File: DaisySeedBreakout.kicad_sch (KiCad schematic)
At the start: 48 parts, among them J2 Conn_01x02, J24 Conn_01x02, J25 Conn_01x02, J26 Conn_02x04, J30 Conn_01x02, J31 Conn_02x04, J32 Conn_01x02, J33 Conn_01x02, J34 Conn_01x02, J35 Conn_01x02, J6 Conn_01x02, J7 Conn_01x02, U10 TPD2EUSB30ADRTR, U11 TPS560200DBVR

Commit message: getting closer
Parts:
- removed C61: 47uF, Capacitor_SMD:C_0805_2012Metric, symbol Device:C
- removed C62, C65: 0.1uF, Capacitor_SMD:C_0402_1005Metric, symbol Device:C
- removed C63, C64: 10uF, Capacitor_SMD:C_0603_1608Metric, symbol Device:C
- removed J26: Conn_02x04, Connector_PinHeader_2.54mm:PinHeader_2x04_P2.54mm_Vertical, symbol 4ms_Connector:Conn_02x04
- removed J32, J33, J34, J7: Conn_01x02, Connector_PinHeader_2.54mm:PinHeader_1x02_P2.54mm_Vertical, symbol 4ms_Connector:Conn_01x02
- removed L1: 10uH 1.9A ASPI-0628-100M-T1, 10uHInductor:ASPI-0628_ASPI-0628-4R7M-T1_ABR, symbol Device:L_Small
- removed R59, R60, R63, R64: TBD, Resistor_SMD:R_0402_1005Metric, symbol Device:R_US
- removed R61: 2.2k, Resistor_SMD:R_0402_1005Metric, symbol Device:R_US
- removed U11: TPS560200DBVR, DBV0005A_N, symbol 2023-10-05_01-44-07:TPS560200DBVR
- added J15: Conn_01x03, Ultralibrarian:PinHeader_1x03_P2.54mm_Vertical_Female, symbol 4ms_Connector:Conn_01x03
- added J16: Conn_02x04, Connector_PinHeader_2.54mm:PinHeader_2x04_P2.54mm_Vertical, symbol 4ms_Connector:Conn_02x04
- renumbered R56 to Z56
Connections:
- net GND: now also H1.1, H2.1, H3.1, H4.1, J15.1 (Pin_1), J16.1 (Pin_1), J16.3 (Pin_3), J16.5 (Pin_5), J16.7 (Pin_7)
- net USB_n: now also J15.3 (Pin_3)
- net USB_p: now also J15.2 (Pin_2)
- net at C57.1, C58.1, CR1.1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: now also J16.2 (Pin_2), J16.4 (Pin_4), J16.6 (Pin_6), J16.8 (Pin_8)
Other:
- sheet Audio Out ports: added none; removed ENABLE_10V_EURO_N, VCC_4V5_36V
- note added: "Make line to Eurorack and Eurorack to line converter. Then make everything line on the product. make CV and gate easy to hook up though? Or provide PCB to convert AI/AO to CV voltages too? Make 12V to 5V module?"
- note removed: "1.16V Threshold 7V Max allowed"
- note removed: "5V"
- note removed: "Current limiting provided by power supply. This is only thing on 5V."
- note removed: "Header to enable Eurorack mode"
- moved on the sheet: C57, C58, C59, C60, CR1, J31, J35, J5, Z56

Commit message: trying grid of female headers to reduce header count and enable plug in modules
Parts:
- removed J16, J31: Conn_02x04, Connector_PinHeader_2.54mm:PinHeader_2x04_P2.54mm_Vertical, symbol 4ms_Connector:Conn_02x04
- removed J24, J25, J30: Conn_01x02, Connector_PinHeader_2.54mm:PinHeader_1x02_P2.54mm_Vertical, symbol 4ms_Connector:Conn_01x02
- added J10, J11, J8, J9: Conn_01x02, 1x2FemaleVertical:PinHeader_1x02_P2.54mm_VerticalFemale, symbol 4ms_Connector:Conn_01x02
- added J17, J19, J23, J26, J27, J28, J29, J7: Pins_02x10_P2.54mm_TH, 2x10FemaleHeader:PinHeader_2x10_P2.54mm_Vertical, symbol Ultralibrarian_modified_symbols:Pins_02x10_P2.54mm_TH
- J2, J35, J6: footprint Connector_PinHeader_2.54mm:PinHeader_1x02_P2.54mm_Vertical -> 1x2FemaleVertical:PinHeader_1x02_P2.54mm_VerticalFemale
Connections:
- net +12V: now also J10.1 (Pin_1), J10.2 (Pin_2), J11.1 (Pin_1), J11.2 (Pin_2)
- net +3.3V: now also J9.1 (Pin_1)
- net Audio Out/AUDIO_OUT_L_EXT: no longer J6.1 (Pin_1)
- net GND: now also J9.2 (Pin_2)
- net at J35.1 (Pin_1), J5.1 (IN1), J5.2 (IN2): now also J6.1 (Pin_1)
- net AI0 renamed CONN_1_AI_DIO0
- net AI1 renamed CONN_2_AI_DIO0
- net AI10 renamed CONN_9_AI_DIO0
- net AI11 renamed CONN_10_AI_DIO0
- net AI2 renamed CONN_3_AI_DIO0
- net AI3 renamed CONN_4_AI_DIO0
- net AI4 renamed CONN_5_AI_DIO0
- net AI5 renamed CONN_6_AI_DIO0
- net AI6 renamed CONN_7_AI_DIO0
- net AI9 renamed CONN_8_AI_DIO0
- net AO0: no longer names the net of A1.29 (DAC_OUT2)
- net AO1: no longer names the net of A1.30 (DAC_OUT1)
- net GPIO_Conn/GPIO_Conn renamed arduino_coprocessor/I2C0_SCL
- net GPIO_Conn1/GPIO_Conn renamed arduino_coprocessor/I2C0_SDA
- net GPIO_Conn11/GPIO_Conn: no longer names the net of A1.12 (I2C1_SCL), R11.2
- net GPIO_Conn11/GPIO_Conn: now also J8.1 (Pin_1)
- net GPIO_Conn12/GPIO_Conn: no longer names the net of A1.13 (I2C1_SDA), R6.2
- net GPIO_Conn12/GPIO_Conn: now also J8.2 (Pin_2)
- net GPIO_Conn2/GPIO_Conn renamed arduino_coprocessor/I2C2_SCL
- net GPIO_Conn3/GPIO_Conn renamed arduino_coprocessor/I2C2_SDA
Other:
- removed sheet AI_GPIO
- removed sheet AI_GPIO1
- removed sheet AI_GPIO10
- removed sheet AI_GPIO11
- removed sheet AI_GPIO12
- removed sheet AI_GPIO13
- removed sheet AI_GPIO14
- removed sheet AI_GPIO15
- removed sheet AI_GPIO16
- removed sheet AI_GPIO17
- removed sheet AI_GPIO18
- removed sheet AI_GPIO19
- removed sheet AI_GPIO2
- removed sheet AI_GPIO3
- removed sheet AI_GPIO4
- removed sheet AI_GPIO5
- removed sheet AI_GPIO6
- removed sheet AI_GPIO7
- removed sheet AI_GPIO8
- removed sheet AI_GPIO9
- removed sheet Analog_out_conn
- removed sheet Analog_out_conn1
- removed sheet GPIO_Conn
- removed sheet GPIO_Conn1
- removed sheet GPIO_Conn11
- removed sheet GPIO_Conn12
- removed sheet GPIO_Conn2
- removed sheet GPIO_Conn3
- removed sheet GPIO_Conn4
- removed sheet GPIO_Conn5
- removed sheet GPIO_Conn6
- removed sheet GPIO_Conn7
- removed sheet GPIO_Conn8
- removed sheet GPIO_Conn9
- note removed: "3.3V"
- note removed: "VOUT_Protected"
- moved on the sheet: J2

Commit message: simplified design, rely on external boards more to cover those cases
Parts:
- removed C57, C58, C59: 0.1uF, Capacitor_SMD:C_0402_1005Metric, symbol Device:C
- removed C60: 47uF, Capacitor_SMD:C_0805_2012Metric, symbol Device:C
- removed CR1: DFLT15A-7, ZDO_POWERDI123_DIO, symbol 2023-10-02_00-55-35:DFLT15A-7
- removed J10, J35, J6: Conn_01x02, 1x2FemaleVertical:PinHeader_1x02_P2.54mm_VerticalFemale, symbol 4ms_Connector:Conn_01x02
- removed J17, J19, J23, J26, J27, J28, J29, J7: Pins_02x10_P2.54mm_TH, 2x10FemaleHeader:PinHeader_2x10_P2.54mm_Vertical, symbol Ultralibrarian_modified_symbols:Pins_02x10_P2.54mm_TH
- removed J18: ~, Ultralibrarian:STX-4235-3-3-N, symbol Ultralibrarian_modified_symbols:STX-4235-3-3-N
- removed J5: ~, Ultralibrarian:BladeFuseHolder, symbol Ultralibrarian_modified_symbols:BladeFuseHolder
- removed R48, R49, R50, R51: 10k, Resistor_SMD:R_0402_1005Metric, symbol Device:R_US
- removed Z56: RSX501LAM20TR, DIO_RB050LAM_ROM, symbol 2023-10-01_23-34-18:RSX501LAM20TR
- added C10, C2, C8: 0.1uF, Capacitor_SMD:C_0402_1005Metric, symbol Device:C
- added J10, J14: Conn_01x03, Ultralibrarian:PinHeader_1x03_P2.54mm_Vertical_Female, symbol 4ms_Connector:Conn_01x03
- added J12, J13: Conn_01x02, 1x2FemaleVertical:PinHeader_1x02_P2.54mm_VerticalFemale, symbol 4ms_Connector:Conn_01x02
- added J5: Conn_02x08, Connector_PinHeader_2.54mm:PinHeader_2x08_P2.54mm_Vertical, symbol 4ms_Connector:Conn_02x08
- added J6: Pins_02x10_P2.54mm_TH, Connector_PinHeader_2.54mm:PinHeader_2x10_P2.54mm_Vertical, symbol Ultralibrarian_modified_symbols:Pins_02x10_P2.54mm_TH
- added J7: Conn_01x10, Connector_PinHeader_2.54mm:PinHeader_1x10_P2.54mm_Vertical, symbol Connector_Generic:Conn_01x10
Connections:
- net ClassD_20W_Amp/OUT_N is gone; now on net GND: J2.2 (Pin_2)
- net ClassD_20W_Amp/OUT_P is gone; now on net Audio Out/AUDIO_OUT_L_EXT: J2.1 (Pin_1)
- net +12V: no longer J11.1 (Pin_1), J11.2 (Pin_2)
- net +3.3V: no longer J9.1 (Pin_1)
- net +3.3VA: now also C10.1, C2.1, C8.1, J10.3 (Pin_3), J14.3 (Pin_3), J7.1 (Pin_1), J7.10 (Pin_10), J7.2 (Pin_2), J7.3 (Pin_3), J7.4 (Pin_4), J7.5 (Pin_5), J7.6 (Pin_6), J7.7 (Pin_7), J7.8 (Pin_8), J7.9 (Pin_9)
- net Audio In Sum/AUDIO_IN_L_CONN: now also J12.1 (Pin_1)
- net Audio In Sum/AUDIO_IN_R_CONN: now also J13.1 (Pin_1)
- net Audio Out/AUDIO_OUT_R_EXT: now also J11.1 (Pin_1)
- net GND: now also J11.2 (Pin_2), J8.2 (Pin_2), C10.2, C2.2, C8.2, J10.1 (Pin_1), J12.2 (Pin_2), J13.2 (Pin_2), J14.1 (Pin_1), J5.1 (P1), J5.11 (GND), J5.13 (-12), J5.15 (-12V), J5.3 (P3), J5.5 (+12V), J5.7 (12V), J5.9 (GND), J6.1, J6.11, J6.13, J6.15, J6.17, J6.19, J6.3, J6.5, J6.7, J6.9
- net DIO2: now reaches A1.12 (I2C1_SCL), R11.2
- net DIO2: now also J5.6 (P6); no longer J8.1 (Pin_1)
- net DIO3: now reaches A1.13 (I2C1_SDA), R6.2
- net DIO3: now also J5.8 (+12V); no longer J8.2 (Pin_2)
- net AO_0: now reaches A1.29 (DAC_OUT2)
- net AO_0: now also J10.2 (Pin_2)
- net AO_1: now reaches A1.30 (DAC_OUT1)
- net AO_1: now also J14.2 (Pin_2)
- net CONN_10_AI_DIO0 renamed AI_9
- net AI_9: now also J6.20
- net CONN_1_AI_DIO0 renamed AI_0
- net AI_0: now also J6.2
- net CONN_2_AI_DIO0 renamed AI_1
- net AI_1: now also J6.4
- net CONN_3_AI_DIO0 renamed AI_2
- net AI_2: now also J6.6
- net CONN_4_AI_DIO0 renamed AI_3
- net AI_3: now also J6.8
- net CONN_5_AI_DIO0 renamed AI_4
- net AI_4: now also J6.10
- net CONN_6_AI_DIO0 renamed AI_5
- net AI_5: now also J6.12
- net CONN_7_AI_DIO0 renamed AI_6
- net AI_6: now also J6.14
- net CONN_8_AI_DIO0 renamed AI_7
- net AI_7: now also J6.16
- net CONN_9_AI_DIO0 renamed AI_8
- net AI_8: now also J6.18
- net RESET_n renamed DIO0
- net DIO0: now also J5.2 (P2)
- net UPDI renamed DIO1
- net DIO1: now also J5.4 (P4)
- net arduino_coprocessor/SPI0_CS renamed DIO4
- net DIO4: now also J5.10 (GND)
- net arduino_coprocessor/SPI0_SCLK renamed DIO5
- net DIO5: now also J5.12 (GND)
- net arduino_coprocessor/UART0_RXD_SPI0_MISO renamed DIO6
- net DIO6: now also J5.14 (-12V)
- net arduino_coprocessor/UART0_TXD_SPI0_MOSI renamed DIO7
- net DIO7: now also J5.16 (P16)
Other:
- removed sheet ClassD_20W_Amp
- removed sheet arduino_coprocessor
- note added: "These two connectors go side by side to make a 3 wide connector"
- note removed: "Audio In"
- note removed: "Audio Out"
- note removed: "Header for a speaker"
- note removed: "VIN"
- moved on the sheet: J15, J2, U10

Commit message: started layout
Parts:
- added J16: Conn_01x02, 1x2FemaleVertical:PinHeader_1x02_P2.54mm_VerticalFemale, symbol 4ms_Connector:Conn_01x02
- A1: footprint Module:Electrosmith_Daisy_Seed -> ElectgrosmithSurfaceMountModule:Electrosmith_Daisy_Seed
- C6: footprint Capacitor_SMD:C_0603_1608Metric -> Capacitor_SMD:C_0402_1005Metric; Specs 0603, 16V -> (none)
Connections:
- net +3.3V: now also J16.1 (Pin_1)
- net +3.3VA: now also C6.1, J8.1 (Pin_1)
- net DIO0: now also A1.12 (I2C1_SCL), R11.2; no longer A1.33 (SAI2_SD_A)
- net DIO1: now also A1.13 (I2C1_SDA), R6.2; no longer A1.34 (SAI2_FS)
- net DIO2: now also A1.8 (SPI1_CS); no longer A1.12 (I2C1_SCL), R11.2
- net DIO3: now also A1.9 (SPI1_SCK); no longer A1.13 (I2C1_SDA), R6.2
- net DIO4: now also A1.10 (SPI1_POCI); no longer A1.8 (SPI1_CS)
- net DIO5: now also A1.11 (SPI1_PICO); no longer A1.9 (SPI1_SCK)
- net DIO6: now also A1.33 (SAI2_SD_A); no longer A1.10 (SPI1_POCI)
- net DIO7: now also A1.34 (SAI2_FS); no longer A1.11 (SPI1_PICO)
- net GND: now also J16.2 (Pin_2)
- net Audio In Sum/AUDIO_IN_R_LOCAL: now reaches J9.1 (Pin_1)
- net +12V: no longer names the net of A1.39 (VIN)
- net +12V: no longer C6.1
- no-connect marks 0 -> 1
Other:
- moved on the sheet: J9

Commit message: periodic update
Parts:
- removed J6: Pins_02x10_P2.54mm_TH, Connector_PinHeader_2.54mm:PinHeader_2x10_P2.54mm_Vertical, symbol Ultralibrarian_modified_symbols:Pins_02x10_P2.54mm_TH
- removed J7: Conn_01x10, Connector_PinHeader_2.54mm:PinHeader_1x10_P2.54mm_Vertical, symbol Connector_Generic:Conn_01x10
- removed J9: Conn_01x02, 1x2FemaleVertical:PinHeader_1x02_P2.54mm_VerticalFemale, symbol 4ms_Connector:Conn_01x02
- added J9: Pins_02x10_P2.54mm_TH, HeadersWithSolderHoles:PinHeader_3x10_P2.54mm_Vertical, symbol 3x10HeaderWithSolderHoles:Pins_03x10_P2.54mm_TH_SolderHoles
- J10, J14, J15: footprint Ultralibrarian:PinHeader_1x03_P2.54mm_Vertical_Female -> HeadersWithSolderHoles:PinHeader_1x03_P2.54mm_Vertical_Female_WithSolderHoles
- J11, J12, J13, J2: footprint 1x2FemaleVertical:PinHeader_1x02_P2.54mm_VerticalFemale -> HeadersWithSolderHoles:PinHeader_1x02_P2.54mm_VerticalFemale_WithSolderHoles
- J5: footprint Connector_PinHeader_2.54mm:PinHeader_2x08_P2.54mm_Vertical -> HeadersWithSolderHoles:PinHeader_2x08_P2.54mm_Vertical_Female
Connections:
- net +3.3V: now also J16.2 (Pin_2); no longer J16.1 (Pin_1)
- net +3.3VA: now also J9.1, J9.10, J9.2, J9.3, J9.4, J9.5, J9.6, J9.7, J9.8, J9.9; no longer J8.1 (Pin_1)
- net AI_0: now also J9.11
- net AI_1: now also J9.12
- net AI_2: now also J9.13
- net AI_3: now also J9.14
- net AI_4: now also J9.15
- net AI_5: now also J9.16
- net AI_6: now also J9.17
- net AI_7: now also J9.18
- net AI_8: now also J9.19
- net AI_9: now also J9.20
- net Audio In/AUDIO_IN_L_CONN: now also J8.2 (Pin_2)
- net DIO0: now also J5.16 (P16); no longer J5.2 (P2)
- net DIO1: now also J5.14 (-12V); no longer J5.4 (P4)
- net DIO2: now also J5.12 (GND); no longer J5.6 (P6)
- net DIO3: now also J5.10 (GND); no longer J5.8 (+12V)
- net DIO4: now also J5.8 (+12V); no longer J5.10 (GND)
- net DIO5: now also J5.6 (P6); no longer J5.12 (GND)
- net DIO6: now also J5.4 (P4); no longer J5.14 (-12V)
- net DIO7: now also J5.2 (P2); no longer J5.16 (P16)
- net GND: now also J16.1 (Pin_1), J9.21, J9.22, J9.23, J9.24, J9.25, J9.26, J9.27, J9.28, J9.29, J9.30; no longer J16.2 (Pin_2), J8.2 (Pin_2)
- net USB_n: now also J15.2 (Pin_2); no longer J15.3 (Pin_3)
- net USB_p: now also J15.3 (Pin_3); no longer J15.2 (Pin_2)
- new net Condensor Microphone/AUDIO_OUT: J8.1 (Pin_1)
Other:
- sheet Audio In Sum renamed Audio In
- sheet Audio In ports: added none; removed AUDIO_IN_L_LOCAL, AUDIO_IN_R_LOCAL
- sheet Audio Out ports: added VCC; removed none
- note added: "Nice Looking LEDs Adjust audio input gain"
- note added: "Short header to feed mic through"
- note removed: "Accelerometer/Magnometer/Gyroscope/Temperature Sensor"
- note removed: "Eurorack +-10V compatibility? Add op amp that can be configured for either?"
- note removed: "Make line to Eurorack and Eurorack to line converter. Then make everything line on the product. make CV and gate easy to hook up though? Or provide PCB to convert AI/AO to CV voltages too? Make 12V to 5V module?"
- note removed: "Microphone"
- note removed: "NIce Looking LEDs"
- note removed: "Power/Battery connector/Input protection"
- note removed: "Speaker Driver"
- note removed: "Sprinkle Decoupling Bulk Decoupling"
- note removed: "These two connectors go side by side to make a 3 wide connector"
- note removed: "USB Host"
- moved on the sheet: C2, C6, C8, J5

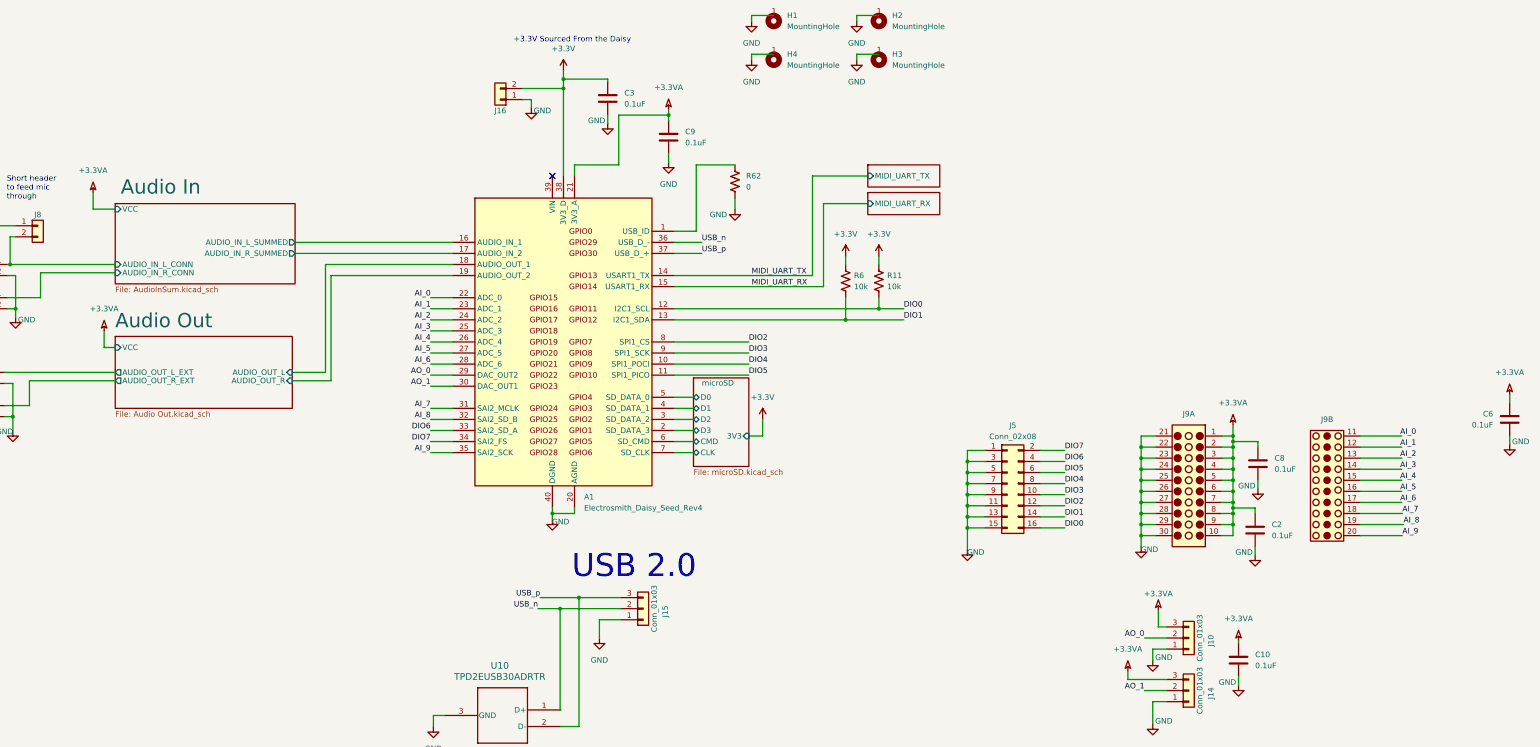
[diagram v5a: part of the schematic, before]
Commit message: added dedicated SPI, UART, I2C connectors
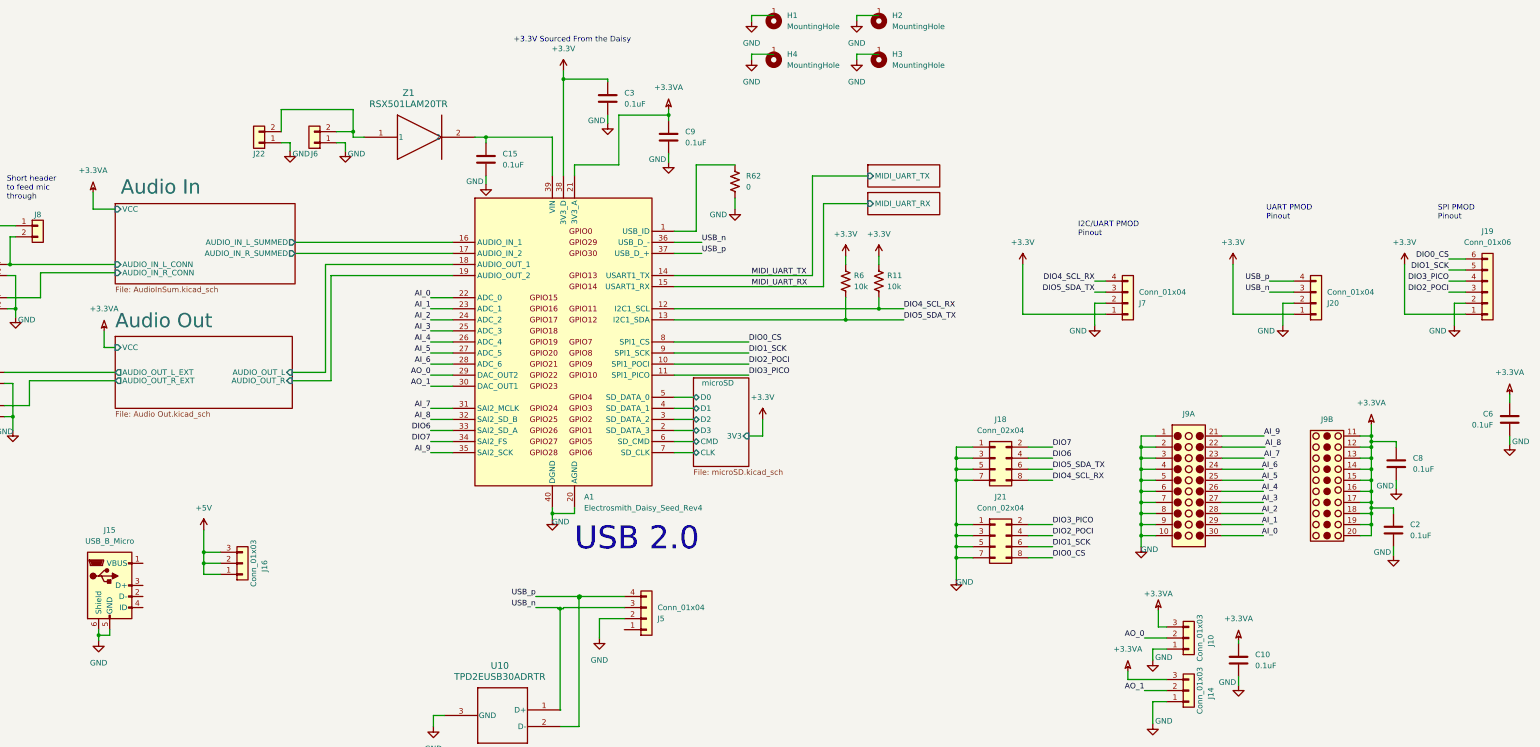
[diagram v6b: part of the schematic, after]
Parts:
- removed J15: Conn_01x03, HeadersWithSolderHoles:PinHeader_1x03_P2.54mm_Vertical_Female_WithSolderHoles, symbol 4ms_Connector:Conn_01x03
- removed J16: Conn_01x02, 1x2FemaleVertical:PinHeader_1x02_P2.54mm_VerticalFemale, symbol 4ms_Connector:Conn_01x02
- removed J5: Conn_02x08, HeadersWithSolderHoles:PinHeader_2x08_P2.54mm_Vertical_Female, symbol 4ms_Connector:Conn_02x08
- added C15: 0.1uF, Capacitor_SMD:C_0603_1608Metric, symbol Device:C
- added J15: USB_B_Micro, Connector_USB:USB_Micro-B_Molex-105017-0001, symbol Connector:USB_B_Micro
- added J16: Conn_01x03, HeadersWithSolderHoles:PinHeader_1x03_P2.54mm_Vertical_Female_WithSolderHoles, symbol 4ms_Connector:Conn_01x03
- added J18, J21: Conn_02x04, HeadersWithSolderHoles:PinHeader_2x04_P2.54mm_Vertical_Female, symbol 4ms_Connector:Conn_02x04
- added J19: Conn_01x06, Ultralibrarian:PinHeader_1x06_P2.54mm_Vertical_Female, symbol Connector_Generic:Conn_01x06
- added J20, J5, J7: Conn_01x04, FemaleHeaders:PinHeader_1x04_P2.54mm_Vertical_Female, symbol Connector_Generic:Conn_01x04
- added J22, J6: Conn_01x02, 1x2FemaleVertical:PinHeader_1x02_P2.54mm_VerticalFemale, symbol 4ms_Connector:Conn_01x02
- added Z1: RSX501LAM20TR, DIO_RB050LAM_ROM, symbol 2023-10-01_23-34-18:RSX501LAM20TR
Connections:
- net +3.3V: now also J19.1 (Pin_1), J20.1 (Pin_1), J7.1 (Pin_1)
- net +3.3VA: now also J9.11, J9.12, J9.13, J9.14, J9.15, J9.16, J9.17, J9.18, J9.19, J9.20; no longer J9.1, J9.10, J9.2, J9.3, J9.4, J9.5, J9.6, J9.7, J9.8, J9.9
- net AI_0: now also J9.30; no longer J9.11
- net AI_1: now also J9.29; no longer J9.12
- net AI_2: now also J9.28; no longer J9.13
- net AI_3: now also J9.27; no longer J9.14
- net AI_4: now also J9.26; no longer J9.15
- net AI_5: now also J9.25; no longer J9.16
- net AI_6: now also J9.24; no longer J9.17
- net AI_7: now also J9.23; no longer J9.18
- net AI_8: now also J9.22; no longer J9.19
- net AI_9: now also J9.21; no longer J9.20
- net DIO6: now also J18.4 (Pin_4)
- net DIO7: now also J18.2 (Pin_2)
- net GND: now also J9.1, J9.10, J9.2, J9.3, J9.4, J9.5, J9.6, J9.7, J9.8, J9.9, C15.2, J15.5 (GND), J15.6 (Shield), J18.1 (Pin_1), J18.3 (Pin_3), J18.5 (Pin_5), J18.7 (Pin_7), J19.2 (Pin_2), J20.2 (Pin_2), J21.1 (Pin_1), J21.3 (Pin_3), J21.5 (Pin_5), J21.7 (Pin_7), J22.1 (Pin_1), J5.2 (Pin_2), J6.1 (Pin_1), J7.2 (Pin_2); no longer J9.21, J9.22, J9.23, J9.24, J9.25, J9.26, J9.27, J9.28, J9.29, J9.30
- net USB_n: now also J20.3 (Pin_3), J5.3 (Pin_3)
- net USB_p: now also J20.4 (Pin_4), J5.4 (Pin_4)
- net at A1.39 (VIN): now also C15.1, Z1.2
- net DIO0 renamed DIO4_SCL_RX
- net DIO4_SCL_RX: now also J18.8 (Pin_8), J7.4 (Pin_4)
- net DIO1 renamed DIO5_SDA_TX
- net DIO5_SDA_TX: now also J18.6 (Pin_6), J7.3 (Pin_3)
- net DIO2 renamed DIO0_CS
- net DIO0_CS: now also J19.6 (Pin_6), J21.8 (Pin_8)
- net DIO3 renamed DIO1_SCK
- net DIO1_SCK: now also J19.5 (Pin_5), J21.6 (Pin_6)
- net DIO4 renamed DIO2_POCI
- net DIO2_POCI: now also J19.3 (Pin_3), J21.4 (Pin_4)
- net DIO5 renamed DIO3_PICO
- net DIO3_PICO: now also J19.4 (Pin_4), J21.2 (Pin_2)
- new net: J22.2 (Pin_2), J6.2 (Pin_2), Z1.1
- new net +5V: J16.1 (Pin_1), J16.2 (Pin_2), J16.3 (Pin_3)
- no-connect marks 1 -> 0
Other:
- note added: "I2C/UART PMOD Pinout"
- note added: "SPI PMOD Pinout"
- note added: "UART PMOD Pinout"
